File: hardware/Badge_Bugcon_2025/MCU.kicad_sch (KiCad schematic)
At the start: 63 parts, among them J1 Flash, J11 +1V8, J12 CODEC, J13 ETH, J14 +3V3, J2 Conn_01x04, SW2 SW_Push, SW3 SW_Push, U6 W25N02KVZEIR, Y1 Crystal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

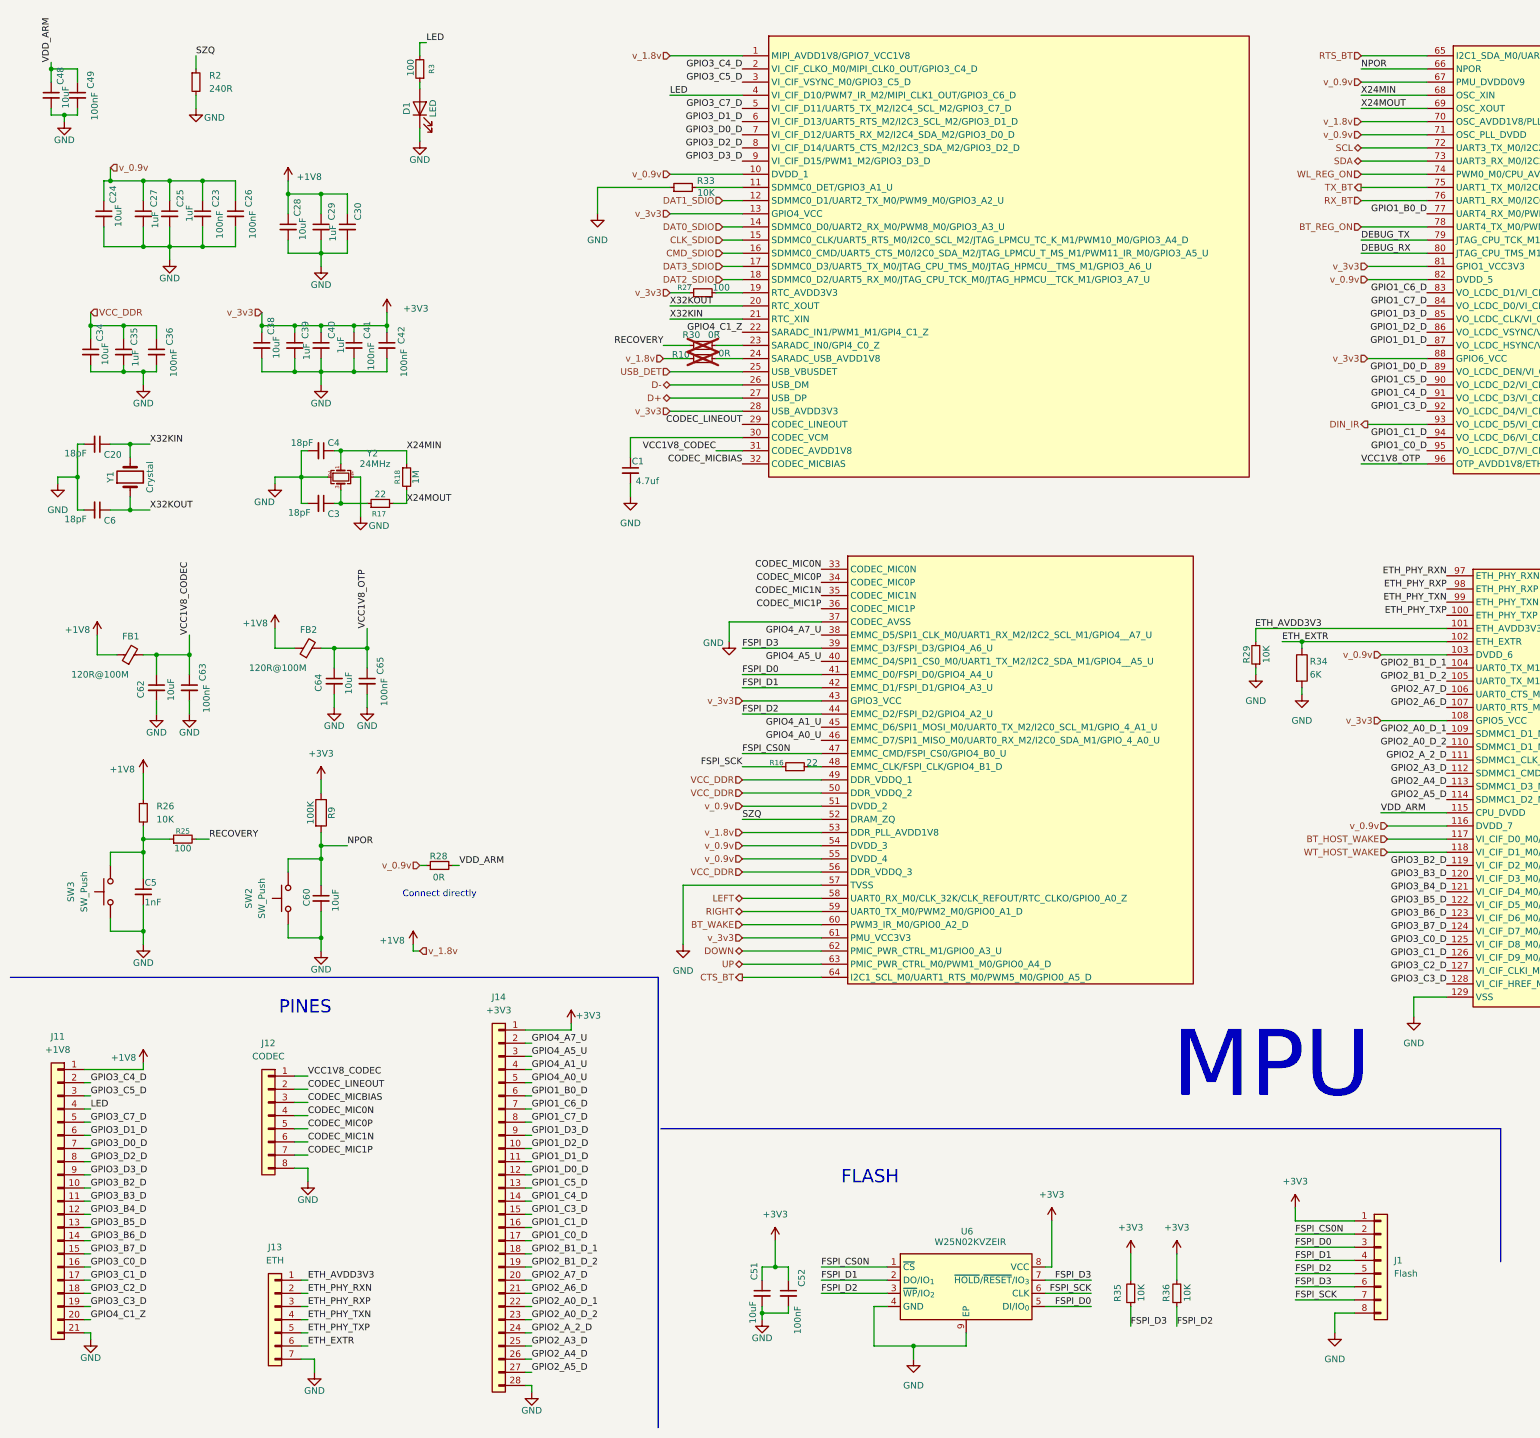
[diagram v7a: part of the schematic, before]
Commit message: feat(Hw):Update_Schematic_And_Floorplan
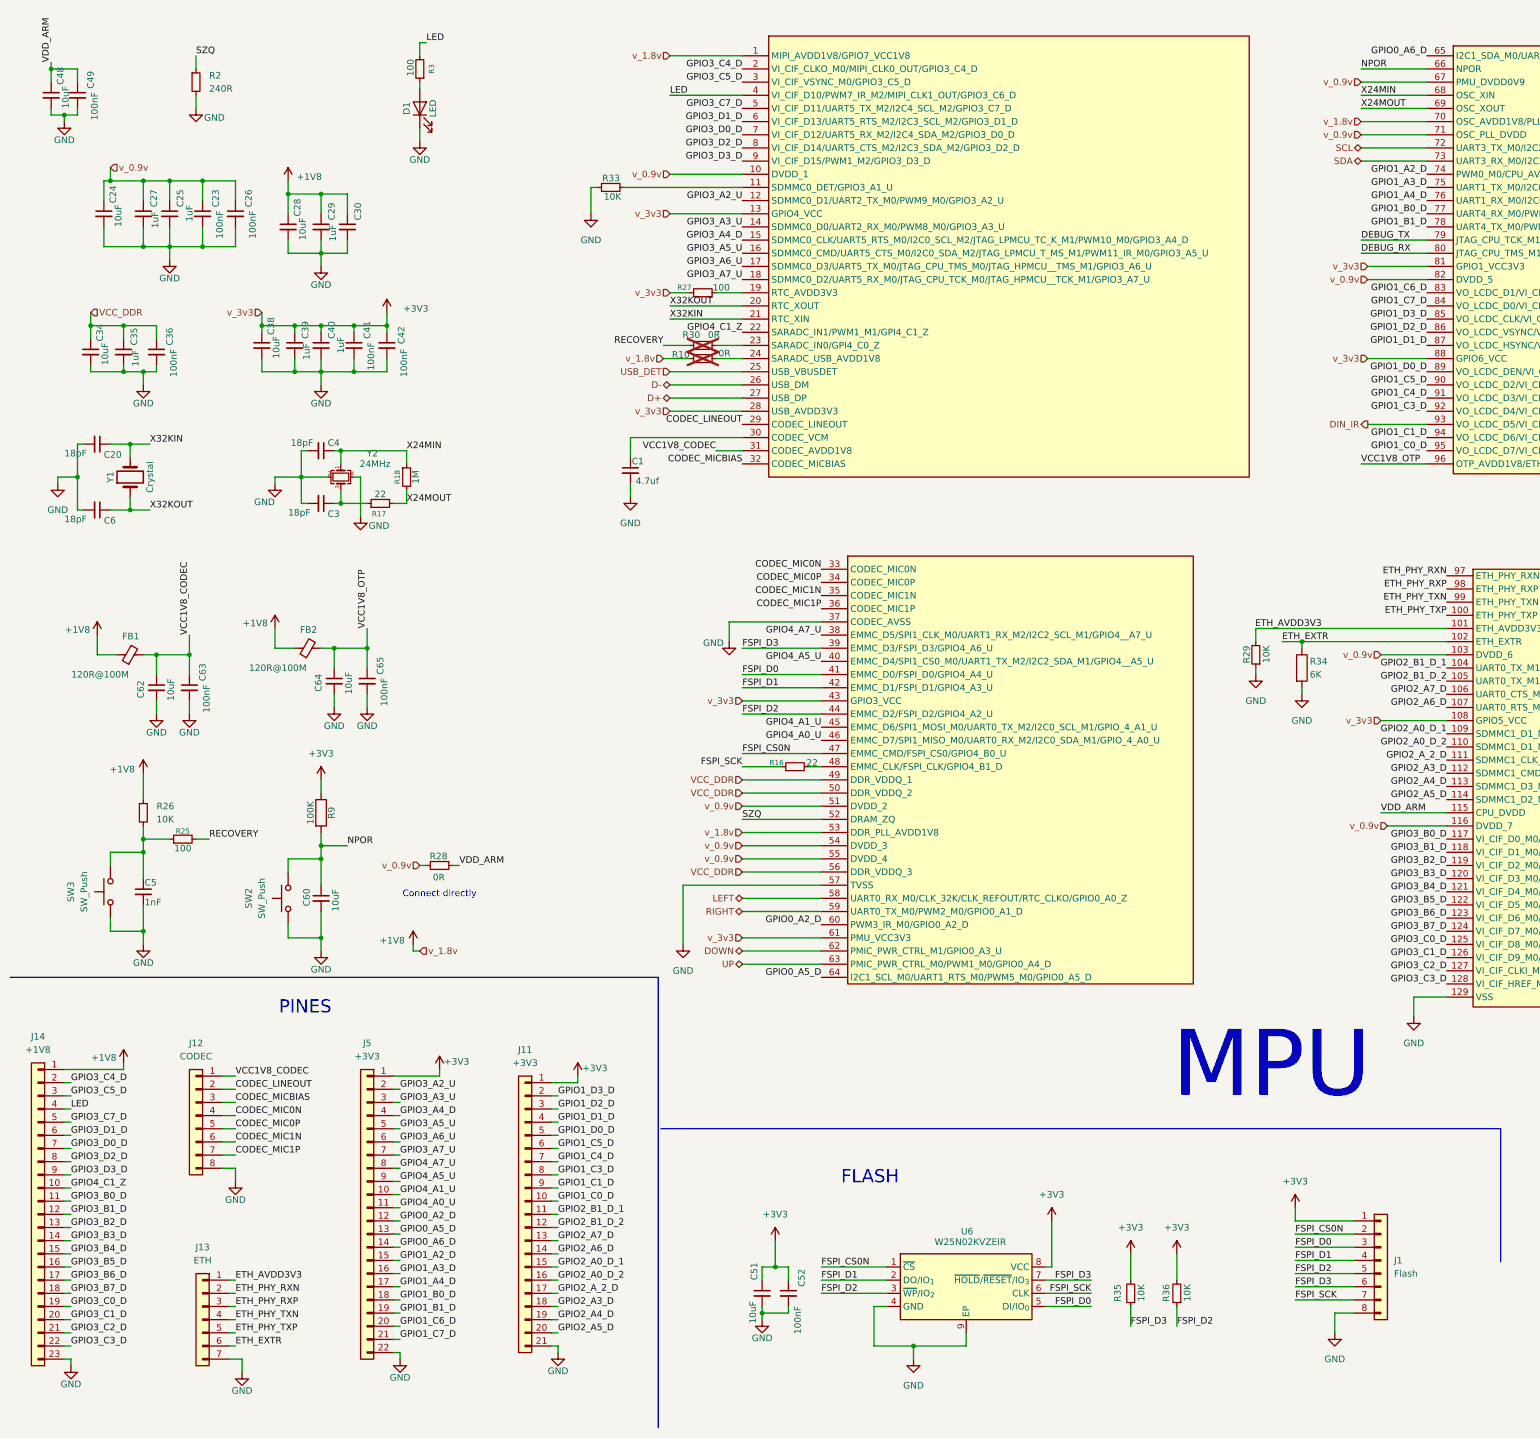
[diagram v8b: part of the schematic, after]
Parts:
- removed J14: +3V3, Connector_PinHeader_2.54mm:PinHeader_1x28_P2.54mm_Vertical, symbol Connector_Generic:Conn_01x28
- added J14: +1V8, Connector_PinHeader_2.54mm:PinHeader_1x23_P2.54mm_Vertical, symbol Connector_Generic:Conn_01x23
- added J5: +3V3, Connector_PinHeader_2.54mm:PinHeader_1x22_P2.54mm_Vertical, symbol Connector_Generic:Conn_01x22
- J1, J12: manf# 87220-8 -> (none)
- J11: value +1V8 -> +3V3; footprint Connector_PinHeader_2.54mm:PinHeader_1x28_P2.54mm_Vertical -> Connector_PinHeader_2.54mm:PinHeader_1x21_P2.54mm_Vertical
- J13: manf# 87224-7 -> (none)
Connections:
- net +1V8: now also J14.1 (Pin_1); no longer J11.1 (Pin_1)
- net +3V3: now also J11.1 (Pin_1), J5.1 (Pin_1)
- net GND: now also J14.23 (Pin_23), J5.22 (Pin_22)
- net GPIO1_B0_D: now also J5.18 (Pin_18)
- net GPIO1_C0_D: now also J11.10 (Pin_10)
- net GPIO1_C1_D: now also J11.9 (Pin_9)
- net GPIO1_C3_D: now also J11.8 (Pin_8)
- net GPIO1_C4_D: now also J11.7 (Pin_7)
- net GPIO1_C5_D: now also J11.6 (Pin_6)
- net GPIO1_C6_D: now also J5.20 (Pin_20)
- net GPIO1_C7_D: now also J5.21 (Pin_21)
- net GPIO1_D0_D: now also J11.5 (Pin_5)
- net GPIO1_D1_D: now also J11.4 (Pin_4)
- net GPIO1_D2_D: now also J11.3 (Pin_3)
- net GPIO1_D3_D: now also J11.2 (Pin_2)
- net GPIO2_A0_D_1: now also J11.15 (Pin_15)
- net GPIO2_A0_D_2: now also J11.16 (Pin_16)
- net GPIO2_A3_D: now also J11.18 (Pin_18)
- net GPIO2_A4_D: now also J11.19 (Pin_19)
- net GPIO2_A5_D: now also J11.20 (Pin_20)
- net GPIO2_A6_D: now also J11.14 (Pin_14)
- net GPIO2_A7_D: now also J11.13 (Pin_13)
- net GPIO2_A_2_D: now also J11.17 (Pin_17)
- net GPIO2_B1_D_1: now also J11.11 (Pin_11)
- net GPIO2_B1_D_2: now also J11.12 (Pin_12)
- net GPIO3_B2_D: now also J14.13 (Pin_13); no longer J11.10 (Pin_10)
- net GPIO3_B3_D: now also J14.14 (Pin_14); no longer J11.11 (Pin_11)
- net GPIO3_B4_D: now also J14.15 (Pin_15); no longer J11.12 (Pin_12)
- net GPIO3_B5_D: now also J14.16 (Pin_16); no longer J11.13 (Pin_13)
- net GPIO3_B6_D: now also J14.17 (Pin_17); no longer J11.14 (Pin_14)
- net GPIO3_B7_D: now also J14.18 (Pin_18); no longer J11.15 (Pin_15)
- net GPIO3_C0_D: now also J14.19 (Pin_19); no longer J11.16 (Pin_16)
- net GPIO3_C1_D: now also J14.20 (Pin_20); no longer J11.17 (Pin_17)
- net GPIO3_C2_D: now also J14.21 (Pin_21); no longer J11.18 (Pin_18)
- net GPIO3_C3_D: now also J14.22 (Pin_22); no longer J11.19 (Pin_19)
- net GPIO3_C4_D: now also J14.2 (Pin_2); no longer J11.2 (Pin_2)
- net GPIO3_C5_D: now also J14.3 (Pin_3); no longer J11.3 (Pin_3)
- net GPIO3_C7_D: now also J14.5 (Pin_5); no longer J11.5 (Pin_5)
- net GPIO3_D0_D: now also J14.7 (Pin_7); no longer J11.7 (Pin_7)
- net GPIO3_D1_D: now also J14.6 (Pin_6); no longer J11.6 (Pin_6)
- net GPIO3_D2_D: now also J14.8 (Pin_8); no longer J11.8 (Pin_8)
- net GPIO3_D3_D: now also J14.9 (Pin_9); no longer J11.9 (Pin_9)
- net GPIO4_A0_U: now also J5.11 (Pin_11)
- net GPIO4_A1_U: now also J5.10 (Pin_10)
- net GPIO4_A5_U: now also J5.9 (Pin_9)
- net GPIO4_A7_U: now also J5.8 (Pin_8)
- net GPIO4_C1_Z: now also J14.10 (Pin_10); no longer J11.20 (Pin_20)
- net LED: now also J14.4 (Pin_4); no longer J11.4 (Pin_4)
- net BT_HOST_WAKE renamed GPIO3_B0_D
- net GPIO3_B0_D: now also J14.11 (Pin_11)
- net BT_REG_ON renamed GPIO1_B1_D
- net GPIO1_B1_D: now also J5.19 (Pin_19)
- net BT_WAKE renamed GPIO0_A2_D
- net GPIO0_A2_D: now also J5.12 (Pin_12)
- net CLK_SDIO renamed GPIO3_A4_D
- net GPIO3_A4_D: now also J5.4 (Pin_4)
- net CMD_SDIO renamed GPIO3_A5_U
- net GPIO3_A5_U: now also J5.5 (Pin_5)
- net CTS_BT renamed GPIO0_A5_D
- net GPIO0_A5_D: now also J5.13 (Pin_13)
- net DAT0_SDIO renamed GPIO3_A3_U
- net GPIO3_A3_U: now also J5.3 (Pin_3)
- net DAT1_SDIO renamed GPIO3_A2_U
- net GPIO3_A2_U: now also J5.2 (Pin_2)
- net DAT2_SDIO renamed GPIO3_A7_U
- net GPIO3_A7_U: now also J5.7 (Pin_7)
- net DAT3_SDIO renamed GPIO3_A6_U
- net GPIO3_A6_U: now also J5.6 (Pin_6)
- net RTS_BT renamed GPIO0_A6_D
- net GPIO0_A6_D: now also J5.14 (Pin_14)
- net RX_BT renamed GPIO1_A4_D
- net GPIO1_A4_D: now also J5.17 (Pin_17)
- net TX_BT renamed GPIO1_A3_D
- net GPIO1_A3_D: now also J5.16 (Pin_16)
- net WL_REG_ON renamed GPIO1_A2_D
- net GPIO1_A2_D: now also J5.15 (Pin_15)
- net WT_HOST_WAKE renamed GPIO3_B1_D
- net GPIO3_B1_D: now also J14.12 (Pin_12)
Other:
- moved on the sheet: J12, J13, R33
